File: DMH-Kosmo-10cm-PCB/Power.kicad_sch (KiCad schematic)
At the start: 14 parts, among them J0 Conn_01x01, J100 IDC_02x05, J101 IDC_02x08

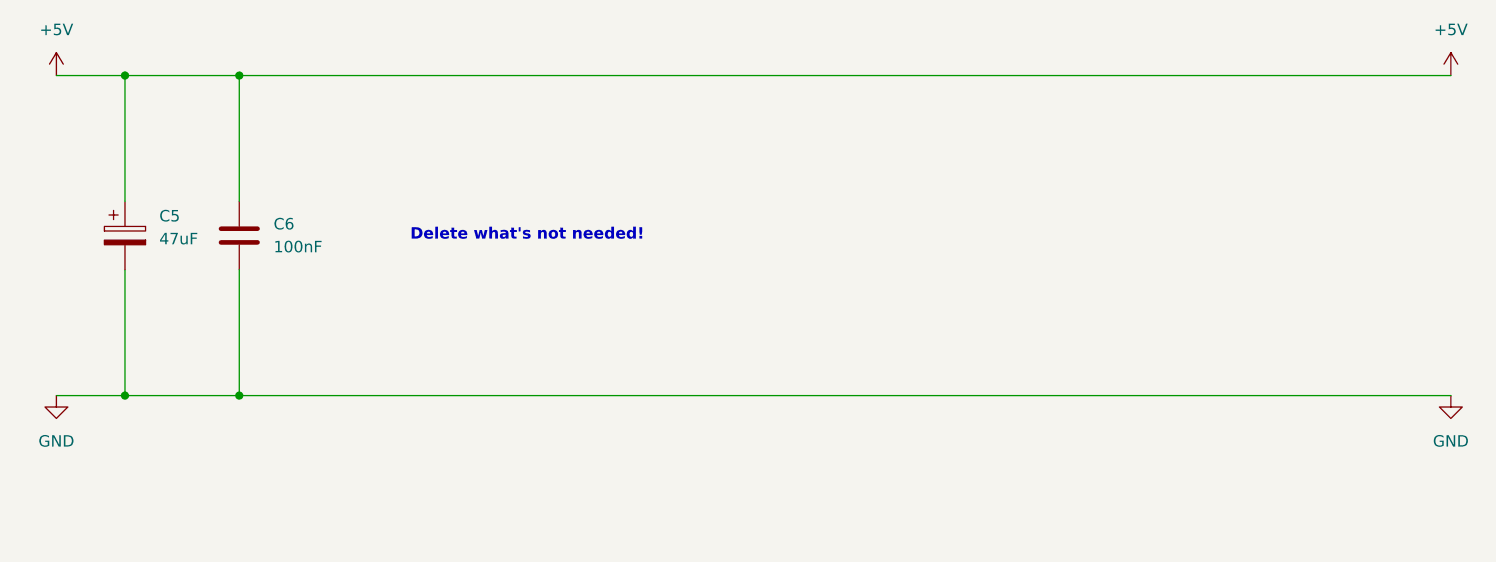
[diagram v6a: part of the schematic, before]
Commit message: Enlarged PCB limits
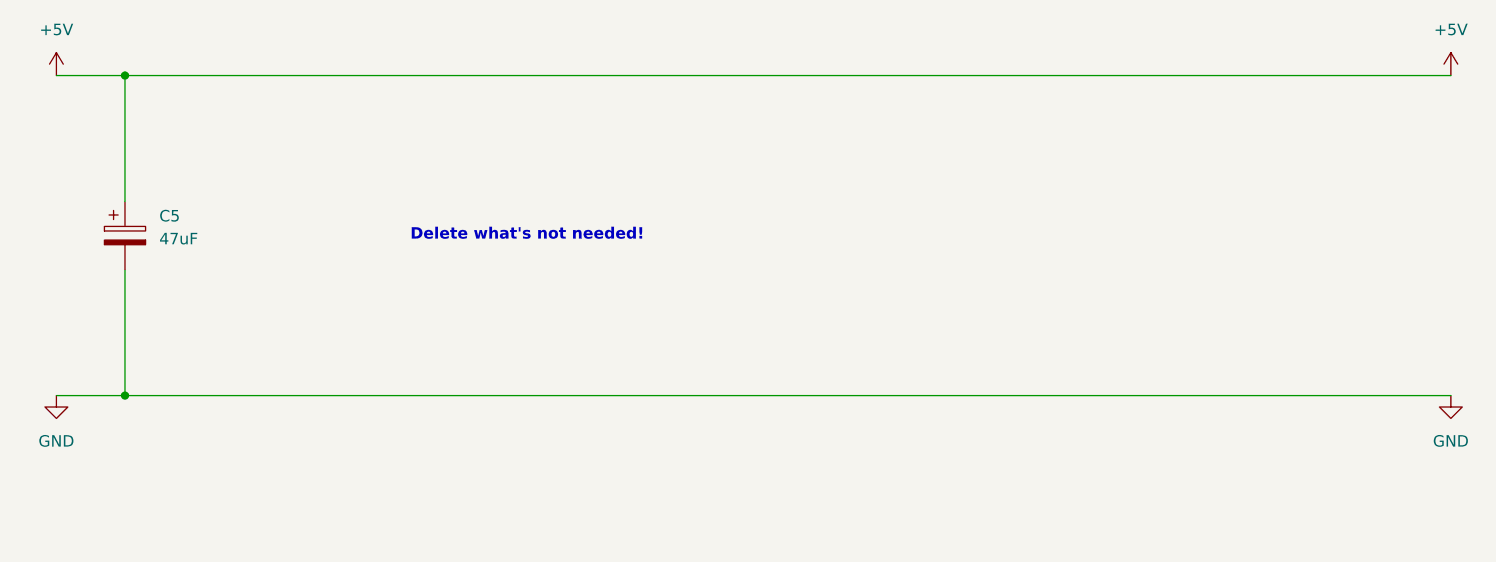
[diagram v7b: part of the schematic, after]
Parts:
- removed C6: 100nF, Capacitor_THT:C_Disc_D4.3mm_W1.9mm_P5.00mm, symbol Device:C
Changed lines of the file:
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@@
 	)
 	(junction
-		(at 38.1 55.88)
-		(diameter 0)
-		(color 0 0 0 0)
-	)
-	(junction
 		(at 63.5 185.42)
 		(diameter 0)
@@
 	)
 	(junction
-		(at 38.1 20.32)
-		(diameter 0)
-		(color 0 0 0 0)
-	)
-	(junction
 		(at 36.83 162.56)
 		(diameter 0)
@@
 	(wire
 		(pts
-			(xy 38.1 55.88) (xy 172.72 55.88)
+			(xy 25.4 55.88) (xy 172.72 55.88)
 		)
 		(stroke
@@
 	(wire
 		(pts
-			(xy 38.1 20.32) (xy 38.1 34.29)
-		)
-		(stroke
-			(width 0)
-			(type default)
-		)
-	)
-	(wire
-		(pts
 			(xy 25.4 95.25) (xy 25.4 104.14)
 		)
@@
 	(wire
 		(pts
-			(xy 38.1 41.91) (xy 38.1 55.88)
-		)
-		(stroke
-			(width 0)
-			(type default)
-		)
-	)
-	(wire
-		(pts
 			(xy 83.82 166.37) (xy 99.06 166.37)
 		)
@@
 	(wire
 		(pts
-			(xy 25.4 20.32) (xy 38.1 20.32)
+			(xy 25.4 20.32) (xy 172.72 20.32)
 		)
 		(stroke
@@
 	(wire
 		(pts
-			(xy 25.4 55.88) (xy 38.1 55.88)
-		)
-		(stroke
-			(width 0)
-			(type default)
-		)
-	)
-	(wire
-		(pts
 			(xy 97.79 180.34) (xy 100.33 180.34)
 		)
@@
 	(wire
 		(pts
-			(xy 38.1 20.32) (xy 172.72 20.32)
-		)
-		(stroke
-			(width 0)
-			(type default)
-		)
-	)
-	(wire
-		(pts
 			(xy 25.4 55.88) (xy 17.78 55.88)
 		)
@@
 					(unit 1)
 				)
-			)
-		)
-	)
-	(symbol
-		(lib_id "Device:C")
-		(at 38.1 38.1 0)
-		(unit 1)
-		(body_style 1)
-		(exclude_from_sim no)
-		(in_bom yes)
-		(on_board yes)
-		(in_pos_files yes)
-		(dnp no)
-		(fields_autoplaced yes)
-		(property "Reference" "C6"
-			(at 41.91 36.8299 0)
-			(show_name no)
-			(do_not_autoplace no)
-			(effects
-				(font
-					(size 1.27 1.27)
-				)
-				(justify left)
-			)
-		)
-		(property "Value" "100nF"
-			(at 41.91 39.3699 0)
-			(show_name no)
-			(do_not_autoplace no)
-			(effects
-				(font
-					(size 1.27 1.27)
-				)
-				(justify left)
-			)
-		)
-		(property "Footprint" "Capacitor_THT:C_Disc_D4.3mm_W1.9mm_P5.00mm"
-			(at 39.0652 41.91 0)
-			(hide yes)
-			(show_name no)
-			(do_not_autoplace no)
-			(effects
-				(font
-					(size 1.27 1.27)
-				)
-			)
-		)
-		(property "Datasheet" ""
-			(at 38.1 38.1 0)
-			(hide yes)
-			(show_name no)
-			(do_not_autoplace no)
-			(effects
-				(font
-					(size 1.27 1.27)
-				)
-			)
-		)
-		(property "Description" "Unpolarized capacitor"
-			(at 38.1 38.1 0)
-			(hide yes)
-			(show_name no)
-			(do_not_autoplace no)
-			(effects
-				(font
-					(size 1.27 1.27)
-				)
-			)
-		)
-		(pin "2"
-		)
-		(pin "1"
-		)
-		(instances
-			(project "DMH-Kosmo-10cm-PCB"
-				(path "/58f4306d-5387-4983-bb08-41a2313fd315/0cdf34b2-39cd-4d9e-981a-97cd34791509"
-					(reference "C6")
-					(unit 1)
-				)
